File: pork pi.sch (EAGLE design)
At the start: 27 parts, among them J1 SJ-2523-SMT-TR, U1 A13

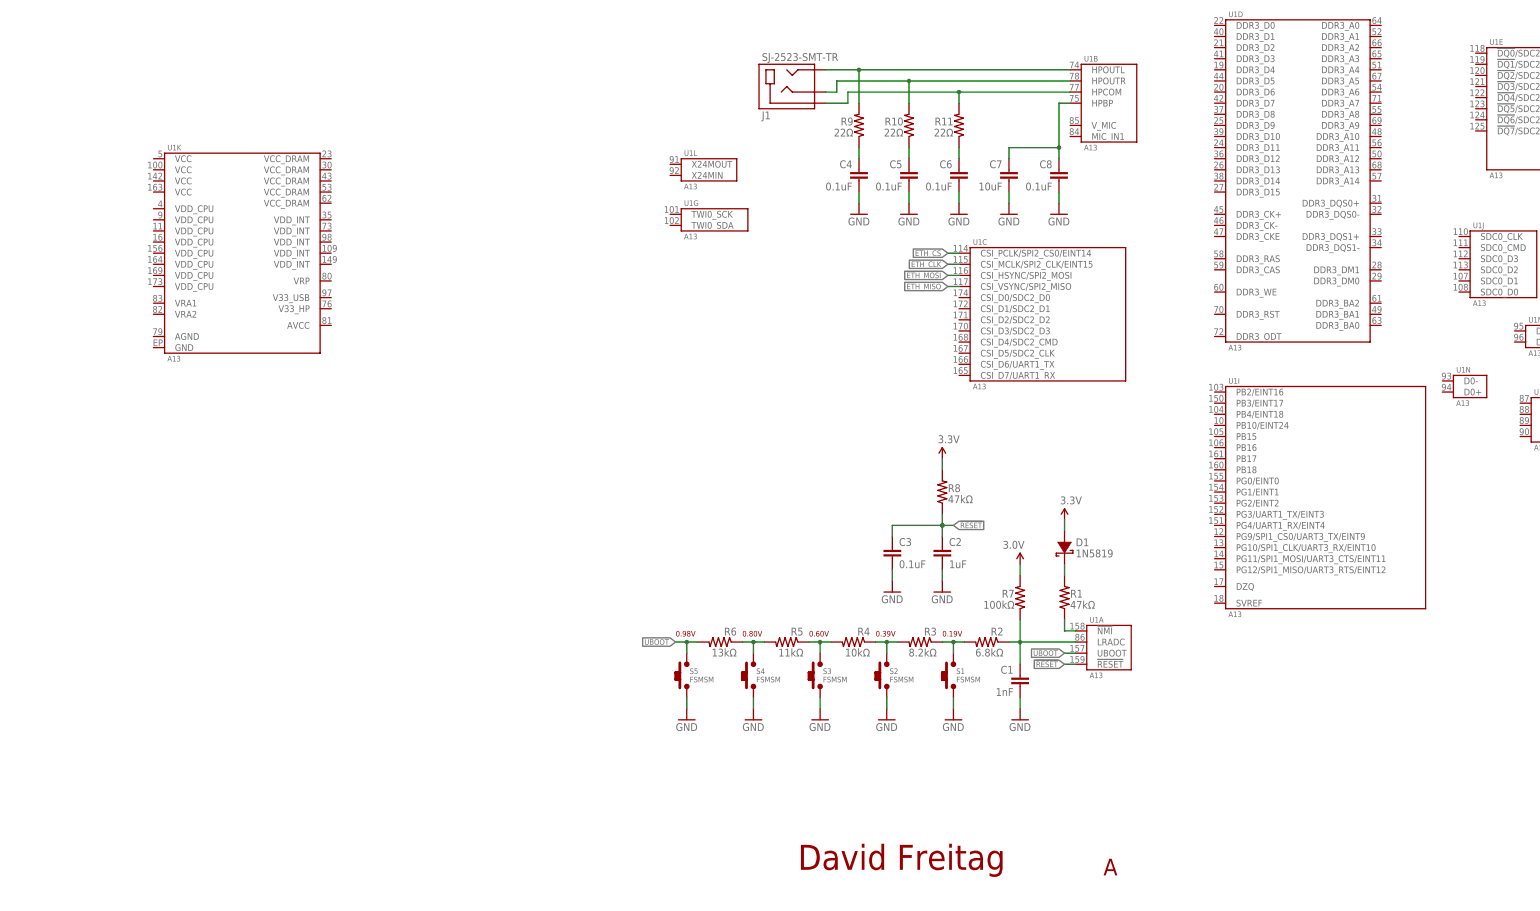
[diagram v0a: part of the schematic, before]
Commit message: Update schematic
Added AXP209 and began routing power management signals
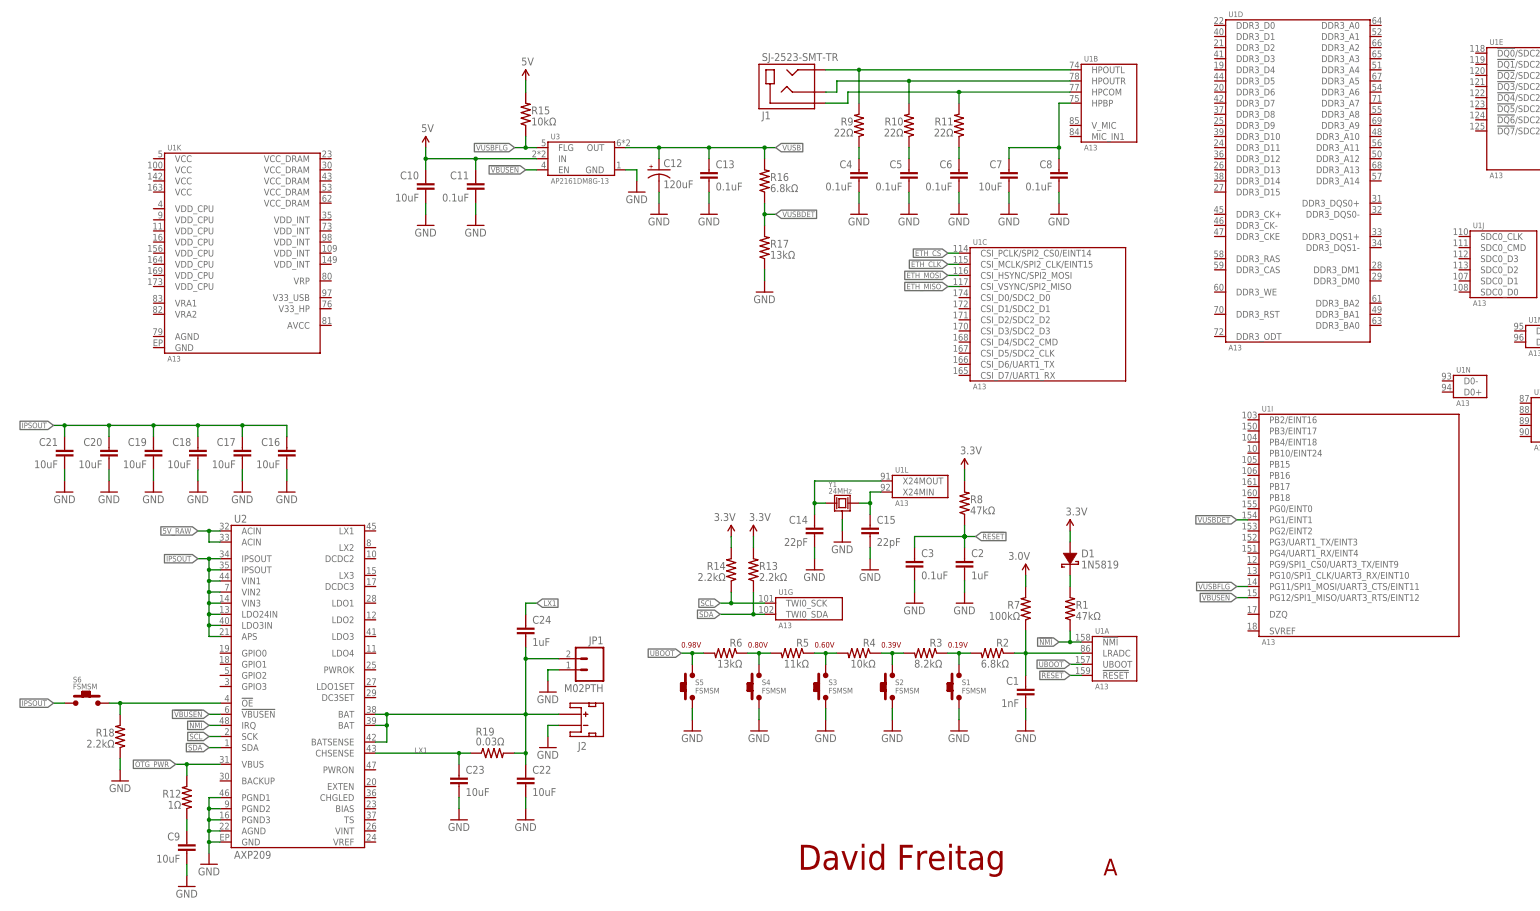
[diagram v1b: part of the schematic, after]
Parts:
- added C10, C16, C17, C18, C19, C20, C21, C22, C23, C9: 10uF, SparkFun-Passives:CAP0603-CAP
- added C11, C13: 0.1uF, SparkFun-Passives:CAP0402-CAP
- added C12: 120uF, Passives:CAP_POL-POLYMER_6.5
- added C14, C15: 22pF, SparkFun-Passives:CAP0402-CAP
- added C24: 1uF, SparkFun-Passives:CAP0402-CAP
- added J2: (no value), SparkFun-Connectors:JST_2MM_MALE
- added JP1: M02PTH, SparkFun-Connectors:M02PTH
- added R12: 1Ω, SparkFun-Passives:RESISTOR0402-RES
- added R13, R14, R18: 2.2kΩ, SparkFun-Passives:RESISTOR0402-RES
- added R15: 10kΩ, SparkFun-Passives:RESISTOR0402-RES
- added R16: 6.8kΩ, SparkFun-Passives:RESISTOR0402-RES
- added R17: 13kΩ, SparkFun-Passives:RESISTOR0402-RES
- added R19: 0.03Ω, SparkFun-Passives:RESISTOR0805-RES
- added S6: FSMSM, TE Connectivity:FSMSM
- added U2: AXP209, X-Powers:AXP209
- added U3: AP2161DM8G-13, Diodes:AP2161DM8G-13
- added Y1: 24MHz, Passives:CRYSTAL-3.2X2.5
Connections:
- new net !NMI: R1.1, U1A.!NMI, U2.IRQ
- new net !VBUSEN: U1I.PG12/SPI1_MISO/UART3_RTS/EINT12, U2.!VBUSEN, U3.EN
- new net 5V: C10.1, C11.1, R15.2, U3.IN
- new net 5V_RAW: U2.ACIN@1, U2.ACIN@2
- new net IPSOUT: C16.1, C17.1, C18.1, C19.1, C20.1, C21.1, S6.P$1, U2.APS, U2.IPSOUT@1, U2.IPSOUT@2, U2.LDO24IN, U2.LDO3IN, U2.VIN1, U2.VIN2, U2.VIN3
- new net LX1: C23.1, C24.1, R19.1, U2.CHSENSE
- new net N$15: C9.1, R12.1
- new net N$16: C14.1, U1L.X24MOUT, Y1.1
- new net N$17: R18.2, S6.P$2, U2.!OE
- new net N$18: C22.1, C24.2, J2.+, JP1.2, R19.2, U2.BAT@1, U2.BAT@2, U2.BATSENSE
- new net OTG_PWR: R12.2, U2.VBUS
- new net SCL: R14.1, U1G.TWI0_SCK, U2.SCK
- new net SDA: R13.1, U1G.TWI0_SDA, U2.SDA
- new net VUSB: C12.+, C13.1, R16.2, U3.OUT
- new net VUSBDET: R16.1, R17.2, U1I.PG1/EINT1
- new net VUSBFLG: R15.1, U1I.PG11/SPI1_MOSI/UART3_CTS/EINT11, U3.FLG
- net 3.3V: now also R13.2, R14.2
- net GND: now also C10.2, C11.2, C12.-, C13.2, C14.2, C15.2, C16.2, C17.2, C18.2, C19.2, C20.2, C21.2, C22.2, C23.2, C9.2, J2.-, JP1.1, R17.1, R18.1, U2.AGND, U2.GND, U2.PGND1, U2.PGND2, U2.PGND3, U3.GND, Y1.GND
- net N$1: now also C15.1, U1L.X24MIN, Y1.2; no longer R1.1, U1A.!NMI
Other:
- moved on the sheet: C1, C2, C3, D1, R1, R2, R3, R4, R5, R6, R7, R8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

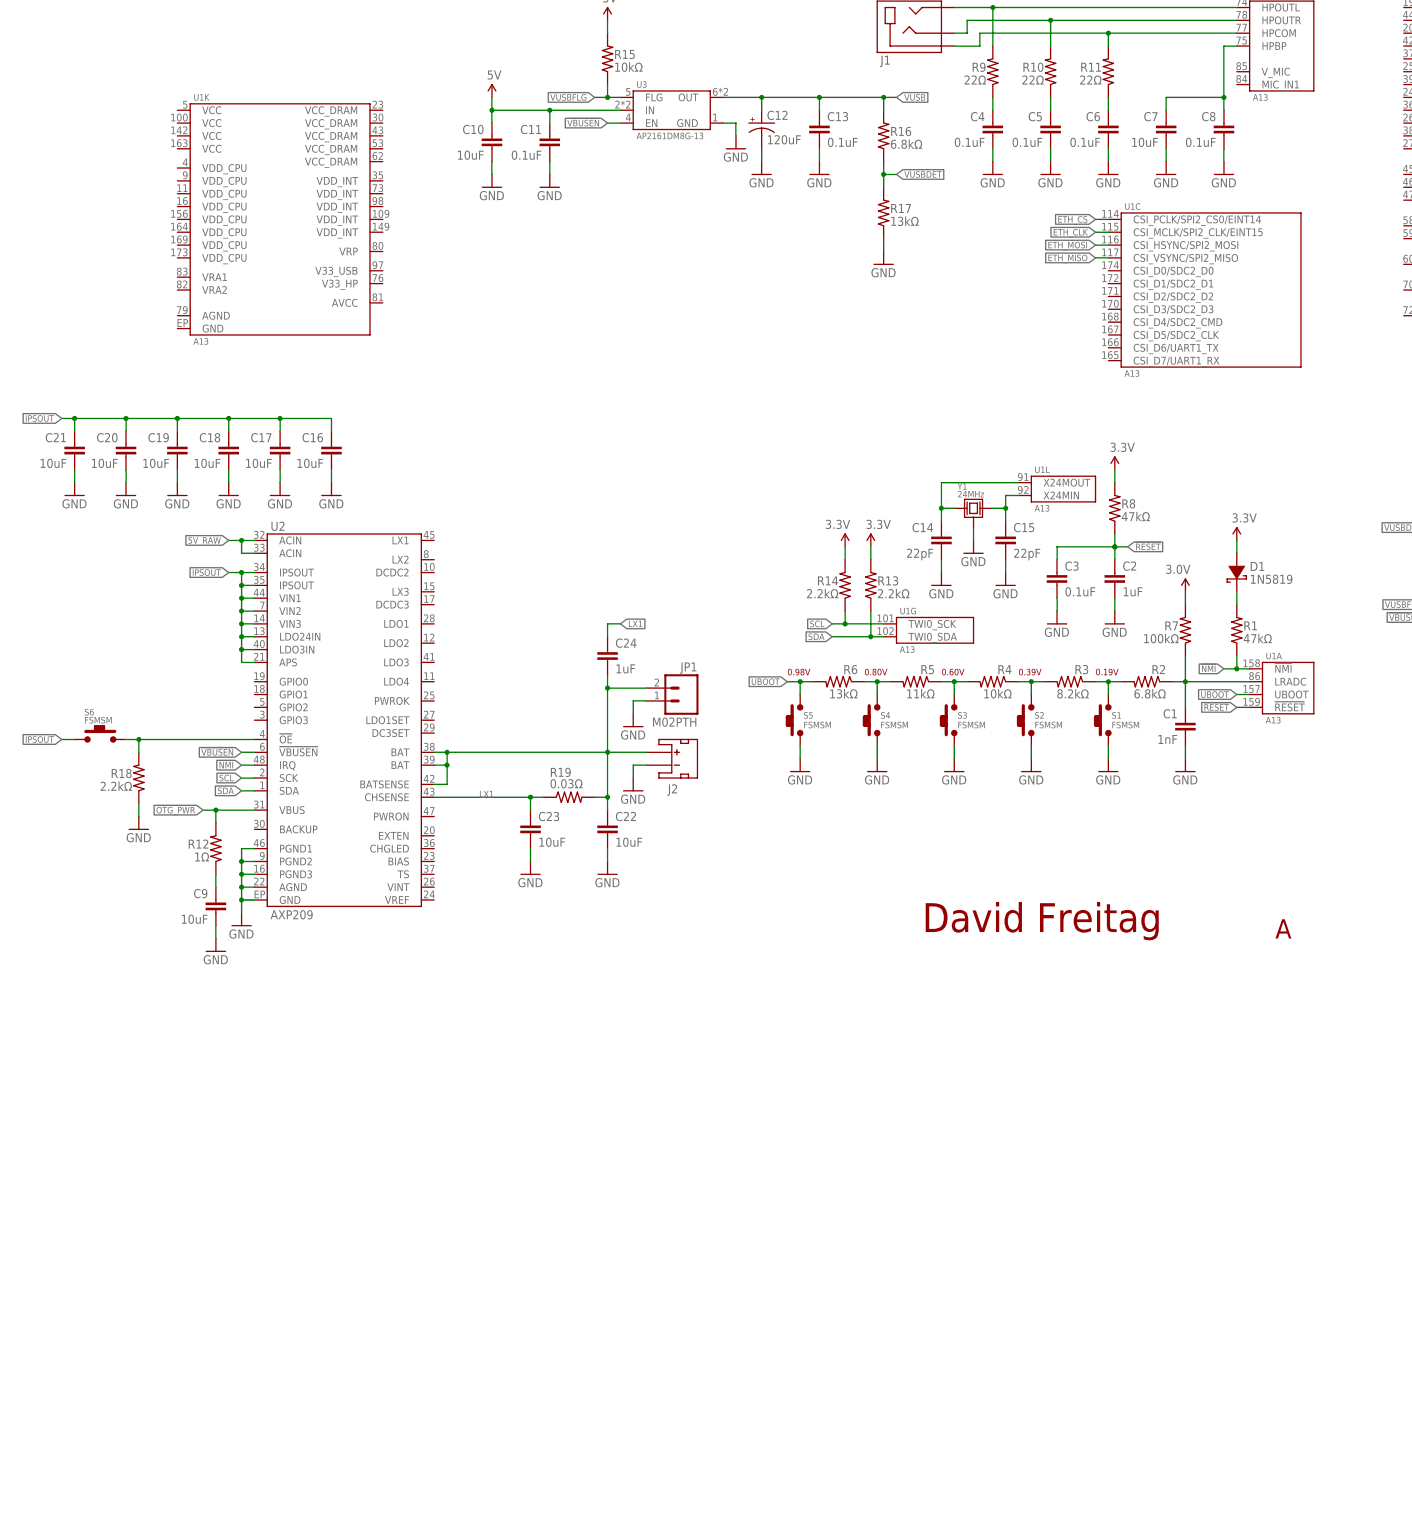
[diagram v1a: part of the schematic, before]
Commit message: Schematic update
Added more signals to AXP209 including inductors
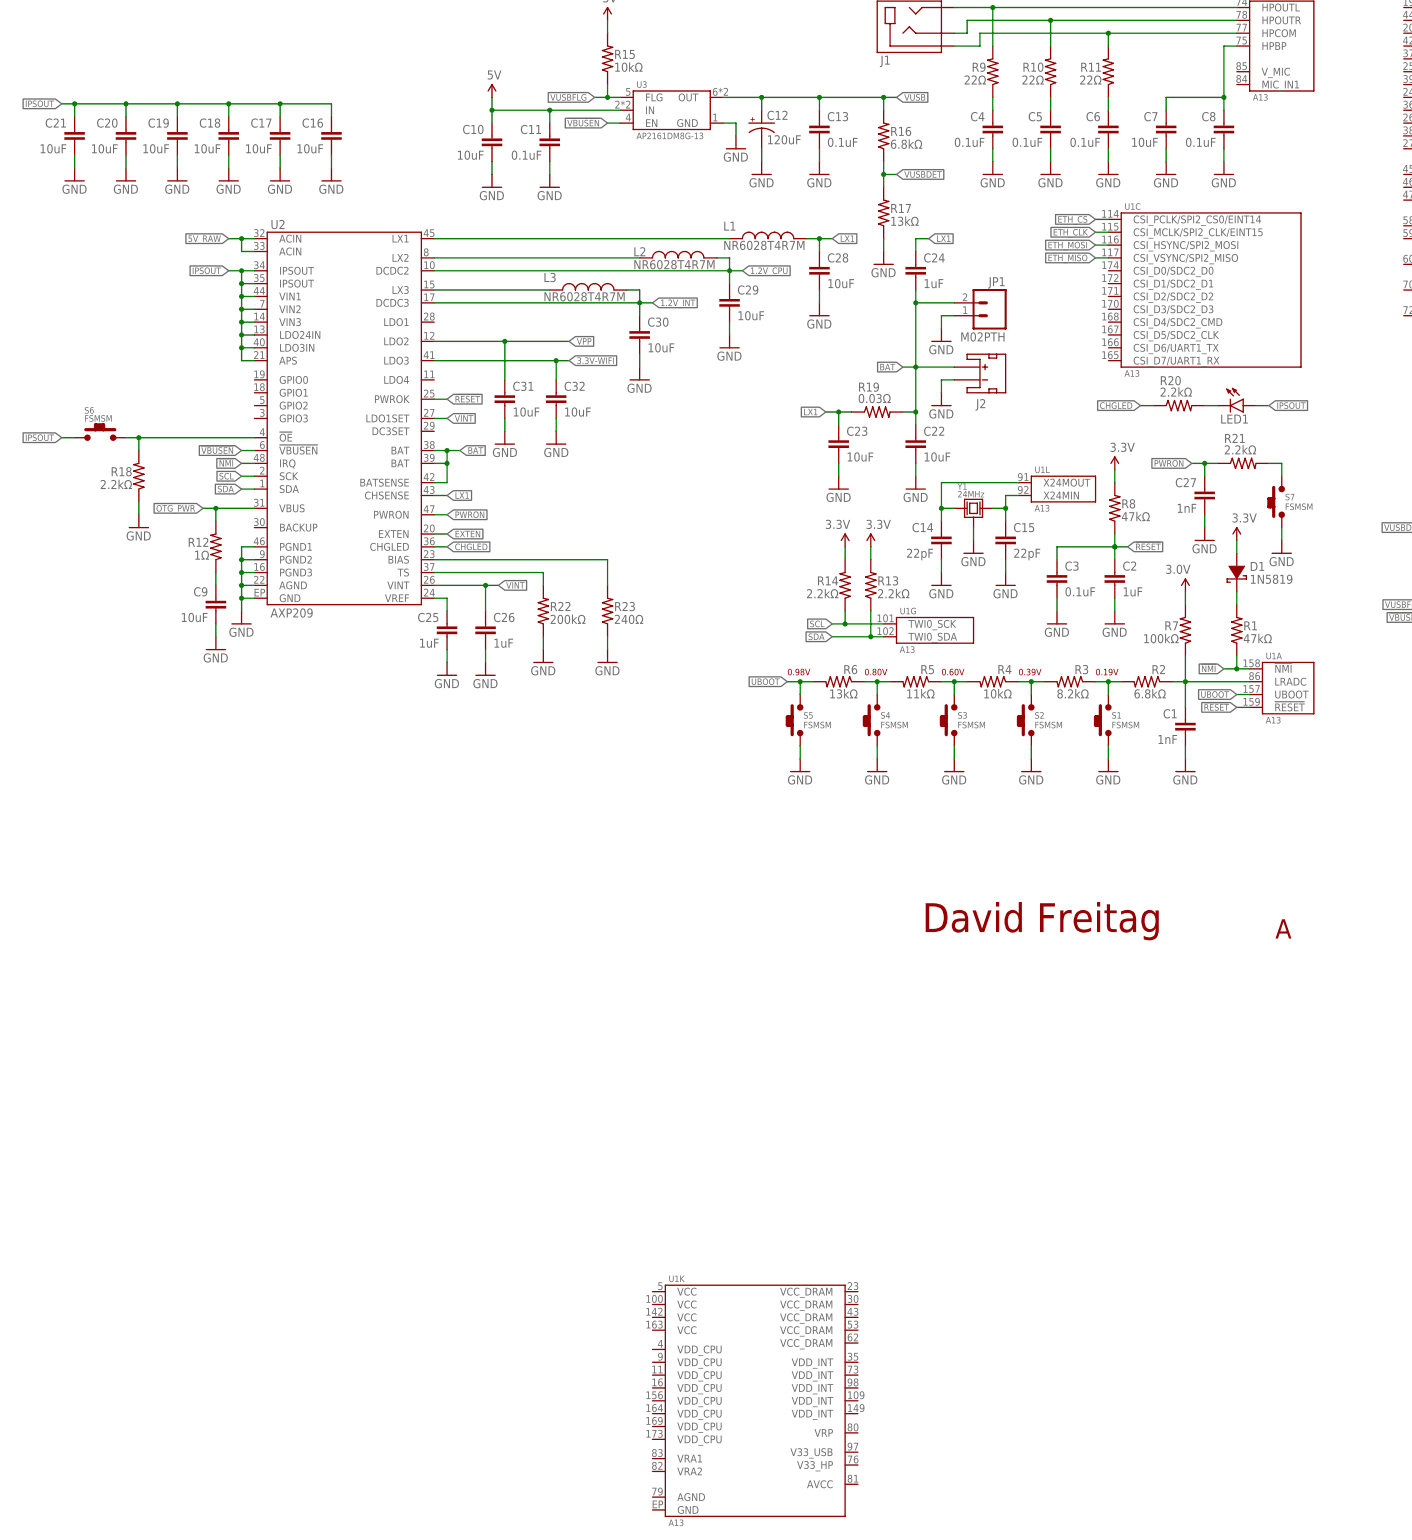
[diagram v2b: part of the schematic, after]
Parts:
- added C25, C26: 1uF, SparkFun-Passives:CAP0402-CAP
- added C27: 1nF, SparkFun-Passives:CAP0402-CAP
- added C28, C29, C30, C31, C32: 10uF, SparkFun-Passives:CAP0603-CAP
- added L1, L2, L3: NR6028T4R7M, Taiyo Yuden:NR6028T4R7M
- added LED1: (no value), SparkFun-LED:LED1206
- added R20, R21: 2.2kΩ, SparkFun-Passives:RESISTOR0402-RES
- added R22: 200kΩ, SparkFun-Passives:RESISTOR0402-RES
- added R23: 240Ω, SparkFun-Passives:RESISTOR0402-RES
- added S7: FSMSM, TE Connectivity:FSMSM
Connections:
- net N$18 renamed BAT
- new net 1.2V_CPU: C29.1, L2.2, U2.DCDC2
- new net 1.2V_INT: C30.1, L3.2, U2.DCDC3
- new net 3.3V-WIFI: C32.1, U2.LDO3
- new net CHGLED: R20.1, U2.CHGLED
- new net EXTEN: U2.EXTEN
- new net N$18: R22.2, U2.TS
- new net N$19: C25.1, U2.VREF
- new net N$20: R21.2, S7.P$2
- new net N$21: LED1.C, R20.2
- new net N$22: R23.2, U2.BIAS
- new net N$23: L1.1, U2.LX1
- new net N$24: L2.1, U2.LX2
- new net N$26: L3.1, U2.LX3
- new net PWRON: C27.1, R21.1, U2.PWRON
- new net VINT: C26.1, U2.LDO1SET, U2.VINT
- new net VPP: C31.1, U2.LDO2
- net !RESET: now also U2.PWROK
- net GND: now also C25.2, C26.2, C27.2, C28.2, C29.2, C30.2, C31.2, C32.2, R22.1, R23.1, S7.P$1
- net IPSOUT: now also LED1.A
- net LX1: now also C28.1, L1.2
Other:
- moved on the sheet: C16, C17, C18, C19, C20, C21, C22, C23, C24, C9, J2, JP1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

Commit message: Schematic update
Added SD card as well as decoupling for main cpu
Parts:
- added C33, C34, C46, C50, C57, C62: 22uF, SparkFun-Passives:CAP0603-CAP
- added C35, C36, C37, C38, C39, C40, C41, C42, C47, C51, C52, C53, C58, C59, C63, C64: 0.1uF, SparkFun-Passives:CAP0402-CAP
- added C43, C44, C45, C48, C54, C55, C56, C60, C61: 10uF, SparkFun-Passives:CAP0603-CAP
- added C49: 1uF, SparkFun-Passives:CAP0402-CAP
- added J3: MICRO-SD, SparkFun-Connectors:MICRO-SD
- added L4: CK2125R47M-T, SparkFun-Passives:INDUCTOR0805
- added R24, R25, R26, R27, R28, R29: 10kΩ, SparkFun-Passives:RESISTOR0402-RES
- added R30: 200kΩ, SparkFun-Passives:RESISTOR0402-RES
- added U4: HC-05, Passives:HC-05
- R22: value 200kΩ -> 240Ω
- R23: value 240Ω -> 200kΩ
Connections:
- net CHGLED renamed N$35
- removed net VPP: C31.1, U2.LDO2
- new net 1.5V_DDR: C60.1, C61.1, C62.1, C63.1, C64.1, U1K.VCC_DRAM@1, U1K.VCC_DRAM@2, U1K.VCC_DRAM@3, U1K.VCC_DRAM@4, U1K.VCC_DRAM@5
- new net N$25: J3.DAT1, R24.1, U1J.SDC0_D1
- new net N$27: J3.DAT0, R25.1, U1J.SDC0_D0
- new net N$28: J3.CLK, U1J.SDC0_CLK
- new net N$29: J3.CMD, R26.1, U1J.SDC0_CMD
- new net N$30: J3.DAT3, R27.1, U1J.SDC0_D3
- new net N$31: J3.DAT2, R28.1, U1J.SDC0_D2
- new net N$32: C49.1, U1K.VRA1
- new net N$33: C33.1, C34.1, J3.VCC, L4.2
- new net N$34: C47.1, C48.1, R30.2, U1K.VRA2
- new net N$36: C53.1, C54.1, U1K.VRP
- new net SDC0_CD: J3.CD, R29.1, U1I.PG0/EINT0
- new net UART1_RX: U1C.CSI_D7/UART1_RX, U4.TX
- new net UART1_TX: U1C.CSI_D6/UART1_TX, U4.RX
- net 1.2V_CPU: now also C39.1, C40.1, C41.1, C42.1, C43.1, C44.1, C45.1, C46.1, U1K.VDD_CPU@1, U1K.VDD_CPU@2, U1K.VDD_CPU@3, U1K.VDD_CPU@4, U1K.VDD_CPU@5, U1K.VDD_CPU@6, U1K.VDD_CPU@7, U1K.VDD_CPU@8
- net 1.2V_INT: now also C55.1, C56.1, C57.1, C58.1, C59.1, U1K.VDD_INT@1, U1K.VDD_INT@2, U1K.VDD_INT@3, U1K.VDD_INT@4, U1K.VDD_INT@5
- net 3.0V: now also C31.1, C50.1, U1K.AVCC, U2.LDO2
- net 3.3V: now also C35.1, C36.1, C37.1, C38.1, C51.1, C52.1, L4.1, R24.2, R25.2, R26.2, R27.2, R28.2, R29.2, U1K.V33_HP, U1K.V33_USB, U1K.VCC@1, U1K.VCC@2, U1K.VCC@3, U1K.VCC@4, U4.3V3
- net GND: now also C33.2, C34.2, C35.2, C36.2, C37.2, C38.2, C39.2, C40.2, C41.2, C42.2, C43.2, C44.2, C45.2, C46.2, C47.2, C48.2, C49.2, C50.2, C51.2, C52.2, C53.2, C54.2, C55.2, C56.2, C57.2, C58.2, C59.2, C60.2, C61.2, C62.2, C63.2, C64.2, J3.GND, J3.SHIELD@1, J3.SHIELD@2, J3.VSS, R30.1, U1K.AGND, U1K.GND, U4.GND@1, U4.GND@2, U4.GND@3
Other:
- moved on the sheet: C10, C11, C12, C13, C16, C17, C18, C19, C20, C21, C22, C23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
